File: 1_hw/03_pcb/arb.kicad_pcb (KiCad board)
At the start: 4 copper layers, 100 x 100 mm, 268 parts, among them J1 TYPE-C-31-M-12, J2 SMA, J3 SMA, J4 BNC, J5 PH-00244, SW1 TS-1187A-B-A-B, SW2 SS-12D02-VG4, SW3 SS-12D02-VG4, U1 TLV70333DBV, U10 LMK1C1103PWR, U11 STM32F446ZETx, U12 ICE40UP5K-SG48ITR, U13 93LC56BT-I_OT, U14 FT2232HL, U15 W25Q128JVSIQ, U16 W25Q128JVSIQ, U17 AD9850, U18 AD9744, U19 LM6171, U2 TLV76133DCY, U20 LM6171, U21 TMUX6104, U22 TPL0401B-10, U23 THS3491, U24 ADG1219BRJZ, U25 LM6171, U26 TMUX6104, U3 TLV70333DBV, U4 LM3880MF-1AA, U5 TLV70312DBV, U6 TLV70325DBV, U7 TPS65131RGE, U8 TPD2E001DRL, U9 ADG1219BRJZ, X1 ASE-10.000MHz, X2 ASE-100.000MHz, Y1 32.768k, Y2 12 MHz

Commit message: MINOR: Layout. Grounds. Misc.
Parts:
- moved R75 41.1 mm to (180.5, 91.7), turned to 0 degrees
- moved R76 38.7 mm to (180.5, 93.5), turned to 0 degrees
- moved C25 1.41 mm to (157.5, 140.0), turned to -90 degrees
- moved C27 1.41 mm to (159.0, 140.0), turned to -90 degrees
- moved C30 1.41 mm to (160.5, 140.0), turned to -90 degrees
- moved C32 1.41 mm to (162.0, 140.0), turned to -90 degrees
- moved C23 1.40 mm to (156.0, 140.0), turned to -90 degrees
- moved C43 0.87 mm to (141.8, 76.3)
- moved C45 0.87 mm to (141.8, 73.8)
- moved Y1 0.87 mm to (144.8, 75.0)
- moved R59 0.61 mm to (110.5, 98.7)
- moved D5 0.15 mm to (109.0, 92.3)
- moved R37 0.15 mm to (104.5, 88.2)
- moved R39 0.15 mm to (113.8, 88.2)
- moved R18 0.11 mm to (164.2, 139.2)
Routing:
- net GND: track 163.9 -> 272.8 mm, vias 106 -> 203
- net 5P0V: track 21.7 -> 69.5 mm, vias 9 -> 13
- net 3P3V_D: track 145.2 -> 179.9 mm, vias 35 -> 43
- net GPIO_UART_RXLED_FTDI_L: track 0.00 -> 34.0 mm
- net Net-(D2-K): track 0.00 -> 29.9 mm
- net GPIO_UART_TXLED_FTDI_L: track 0.00 -> 28.8 mm
- net Net-(D3-A): track 0.00 -> 20.4 mm
- net Net-(U7-ENN): track 0.00 -> 12.9 mm
- net Net-(U7-FBP): track 0.00 -> 7.85 mm
- net Net-(U11-PC15): track 0.00 -> 7.75 mm
- net Net-(U18-MODE): track 0.00 -> 7.75 mm
- net Net-(U11-PC14): track 0.00 -> 7.71 mm
- net Net-(D3-K): track 0.00 -> 7.53 mm
- net Net-(U7-FBN): track 0.00 -> 7.21 mm
- net Net-(D2-A): track 0.00 -> 5.88 mm
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
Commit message: FEAT: Finished with Power and GND Layout.
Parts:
- moved C94 0.51 mm to (109.2, 103.9)
- moved R36 0.38 mm to (121.4, 127.7)
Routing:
- net 3P3V_D: track 179.9 -> 207.6 mm, vias 43 -> 51
- net 5P0V: track 69.5 -> 90.1 mm, vias 13 -> 17
- net GND: track 272.8 -> 277.7 mm, vias 203 -> 207
- net Net-(D2-A): track 5.88 -> 9.61 mm
- net Net-(U11-VCAP_1): track 0.00 -> 1.94 mm
- net 3P3V_A: track 186.8 -> 188.8 mm

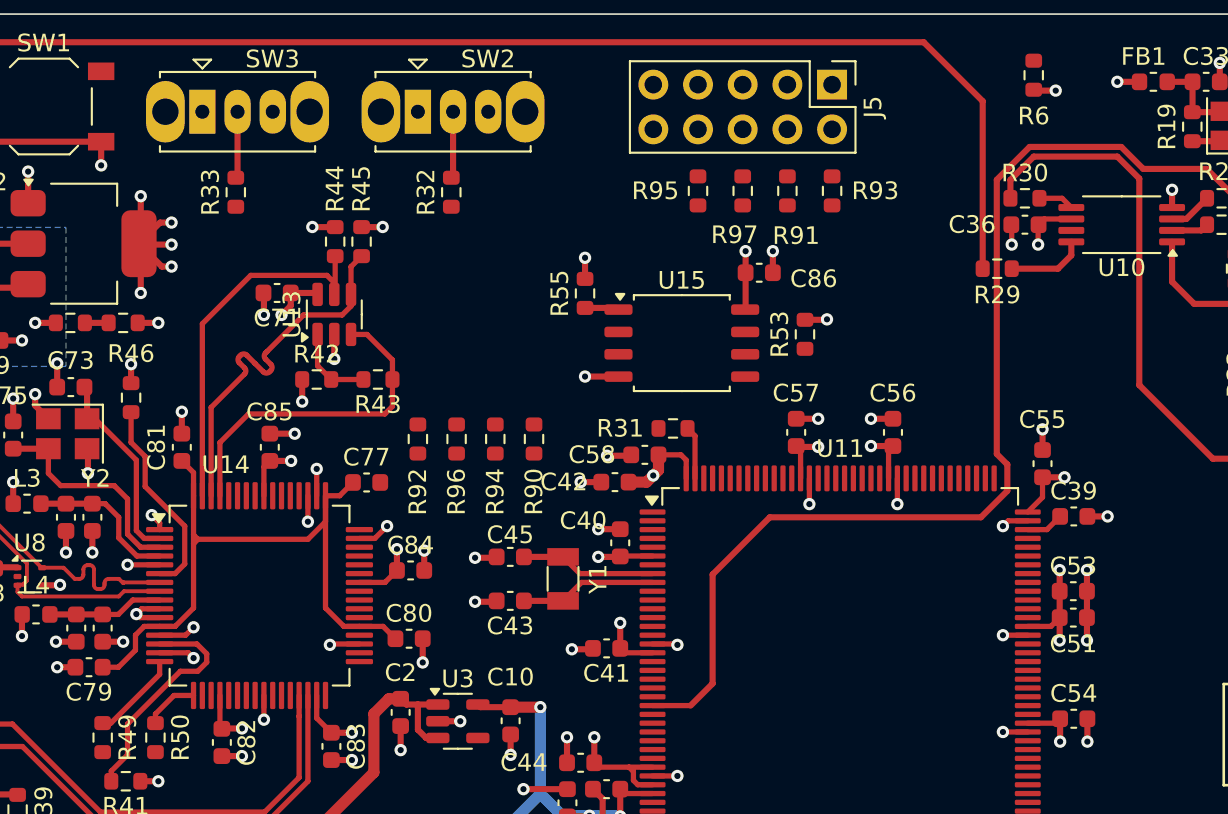
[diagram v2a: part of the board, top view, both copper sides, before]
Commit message: MINOR: Layout, JTAG complete.
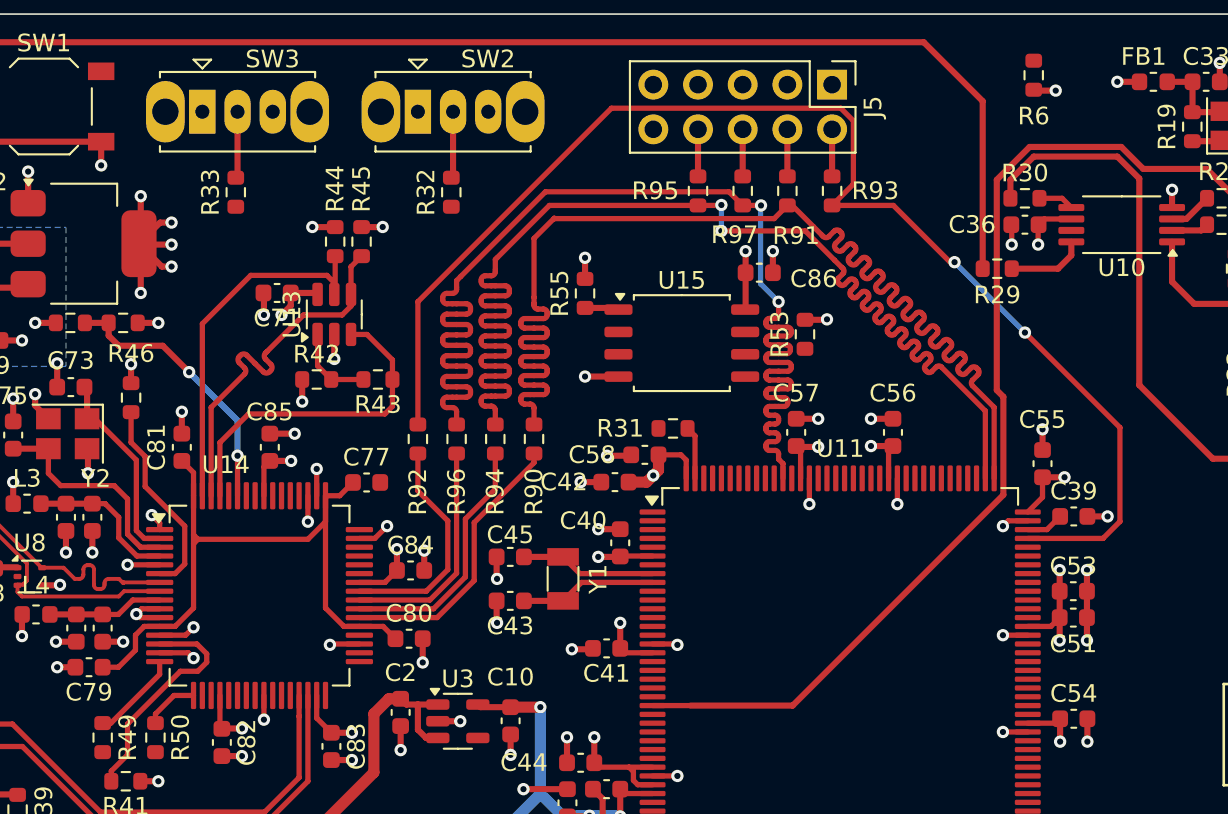
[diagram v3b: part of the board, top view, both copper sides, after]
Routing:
- net JTAG_MCU_TDI_3P3: track 0.00 -> 75.2 mm, vias 0 -> 2
- net JTAG_MCU_TMS_3P3: track 0.00 -> 74.5 mm, vias 0 -> 2
- net JTAG_MCU_TCK_3P3: track 0.00 -> 73.9 mm
- net JTAG_MCU_TDO_3P3: track 0.00 -> 73.9 mm, vias 0 -> 2
- net JTAG_FTDI_TCK_3P3: track 0.00 -> 16.0 mm
- net JTAG_FTDI_TDI_3P3: track 0.00 -> 14.5 mm
- net Net-(U14-BCBUS7): track 1.35 -> 15.7 mm, vias 0 -> 2
- net JTAG_FTDI_TDO_3P3: track 0.00 -> 13.0 mm
- net JTAG_FTDI_TMS_3P3: track 0.00 -> 12.8 mm
- net CLK_10MHZ_DIST_MCU_3P3: track 62.4 -> 58.5 mm
- net JTAG_CON_TMS_3P3: track 0.00 -> 2.67 mm
- net JTAG_CON_TDO_3P3: track 0.00 -> 2.67 mm
- net JTAG_CON_TDI_3P3: track 0.00 -> 2.67 mm
- net JTAG_CON_TCK_3P3: track 0.00 -> 2.67 mm

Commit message: MINOR: Layout, I2C Potentiometer, QSPI MCU Memory.
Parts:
- moved R53 5.64 mm to (154.7, 65.3), turned to 0 degrees
- moved C38 0.50 mm to (169.0, 93.3)
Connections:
- U11 pad 136: I2C_SCL_MCU_POT_3P3 -> unconnected-(U11-PB6-Pad136)
- U11 pad 137: I2C_SDA_MCU_POT_3P3 -> unconnected-(U11-PB7-Pad137)
- U11 pad 69: SPI_SCLK_MCU_FPGA_3P3 -> I2C_SCL_MCU_POT_3P3
- U11 pad 70: unconnected-(U11-PB11-Pad70) -> I2C_SDA_MCU_POT_3P3
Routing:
- net GPIO_BOOT1_SW_MCU_3P3_L: track 0.00 -> 71.7 mm, vias 0 -> 3
- net I2C_SDA_MCU_POT_3P3: track 0.00 -> 69.1 mm, vias 0 -> 2
- net I2C_SCL_MCU_POT_3P3: track 0.00 -> 68.4 mm, vias 0 -> 2
- net QSPI_NCS_MCU_FLASH_3P3: track 1.94 -> 47.8 mm, vias 0 -> 2
- net GPIO_BOOT0_SW_MCU_3P3_L: track 0.00 -> 30.0 mm, vias 0 -> 2
- net QSPI_IO1_MCU_FLASH_3P3: track 0.00 -> 27.2 mm, vias 0 -> 2
- net QSPI_IO3_MCU_FLASH_3P3: track 0.00 -> 23.4 mm, vias 0 -> 2
- net QSPI_IO0_MCU_FLASH_3P3: track 0.00 -> 21.5 mm, vias 0 -> 2
- net QSPI_IO2_MCU_FLASH_3P3: track 0.00 -> 15.8 mm
- net GND: track 277.7 -> 278.2 mm

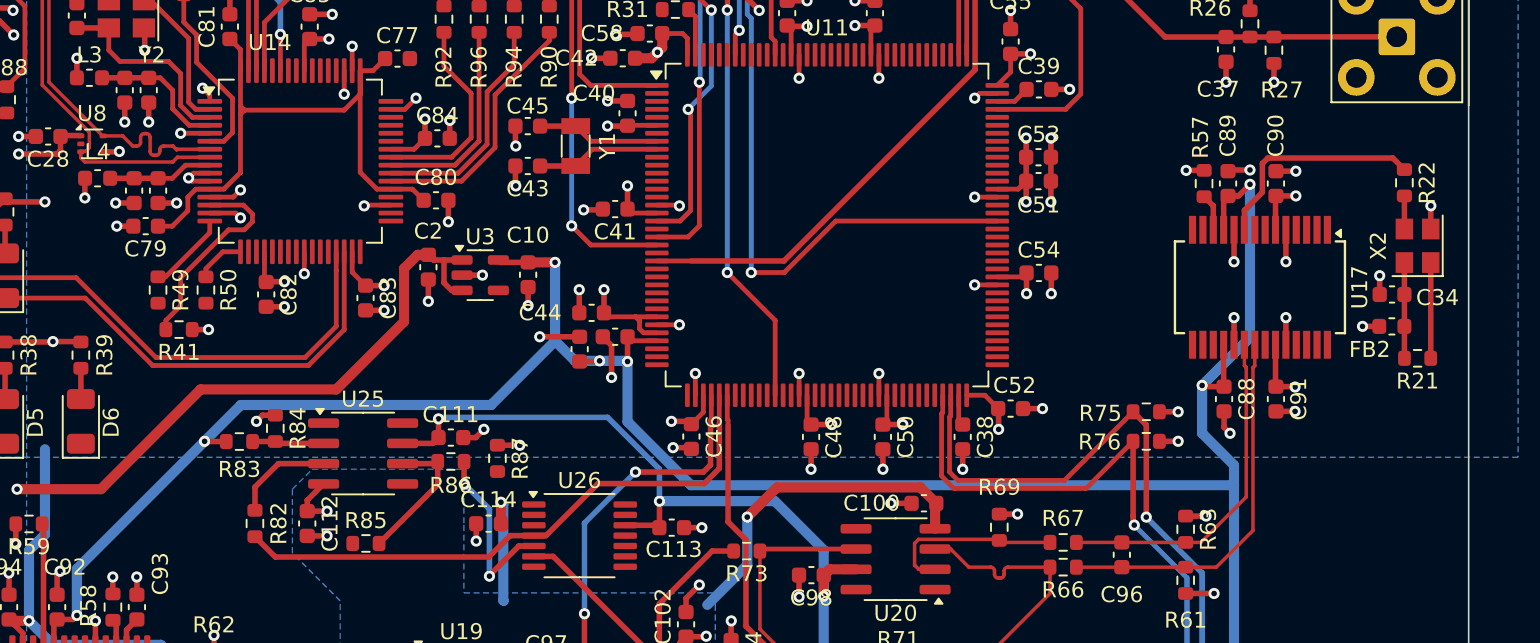
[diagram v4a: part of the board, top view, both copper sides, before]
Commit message: MINOR: Layout, working on SPI / QSPI. Currently mixed up.
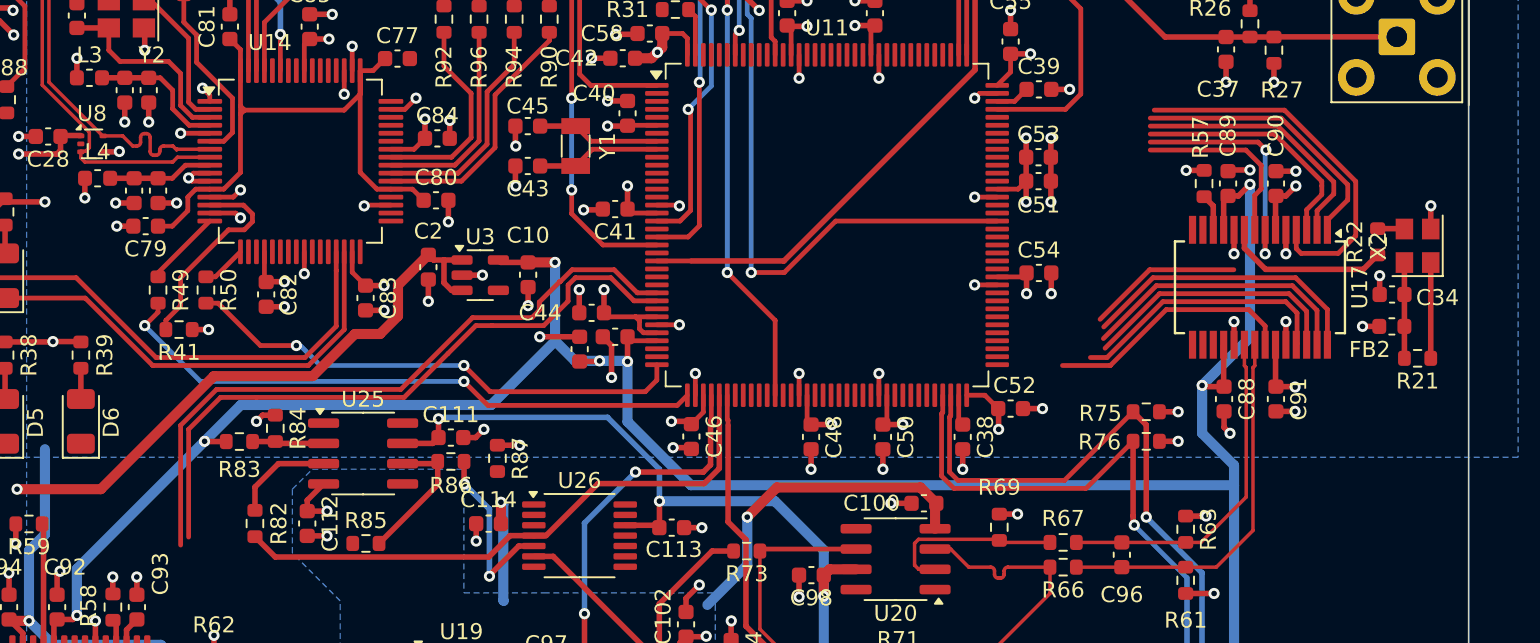
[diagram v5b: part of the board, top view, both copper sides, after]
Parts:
- moved R22 4.06 mm to (195.0, 81.0), turned to 90 degrees
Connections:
- U11 pad 74: unconnected-(U11-PB13-Pad74) -> SPI_SCLK_MCU_FPGA_3P3
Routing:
- net SPI_MOSI_MCU_FPGA_3P3: track 0.00 -> 42.3 mm
- net SPI_MISO_FPGA_MCU_3P3: track 0.00 -> 41.2 mm
- net UART_FTDITX_MCURX_3P3: track 0.00 -> 38.1 mm, vias 0 -> 2
- net UART_MCUTX_FTDIRX_3P3: track 0.00 -> 31.8 mm, vias 0 -> 2
- net GPIO_D0_MCU_DDS_3P3: track 0.00 -> 23.4 mm
- net GPIO_FQ-UD_MCU_DDS_3P3: track 0.00 -> 21.2 mm
- net GPIO_D4_MCU_DDS_3P3: track 0.00 -> 18.3 mm
- net GPIO_D5_MCU_DDS_3P3: track 0.00 -> 17.6 mm
- net GPIO_D3_MCU_DDS_3P3: track 0.00 -> 17.5 mm
- net GPIO_D7_MCU_DDS_3P3: track 0.00 -> 16.7 mm
- net GPIO_D6_MCU_DDS_3P3: track 0.00 -> 16.6 mm
- net GPIO_D2_MCU_DDS_3P3: track 0.00 -> 16.4 mm
- net GPIO_RST_MCU_DDS_3P3: track 0.00 -> 15.7 mm
- net GPIO_W-CLK_MCU_DDS_3P3: track 0.00 -> 15.5 mm, vias 0 -> 2
- net GPIO_D1_MCU_DDS_3P3: track 0.00 -> 15.4 mm
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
